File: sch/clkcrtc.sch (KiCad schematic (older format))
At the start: 26 parts, among them Q1 16 MHz, Q2 13.333 MHz

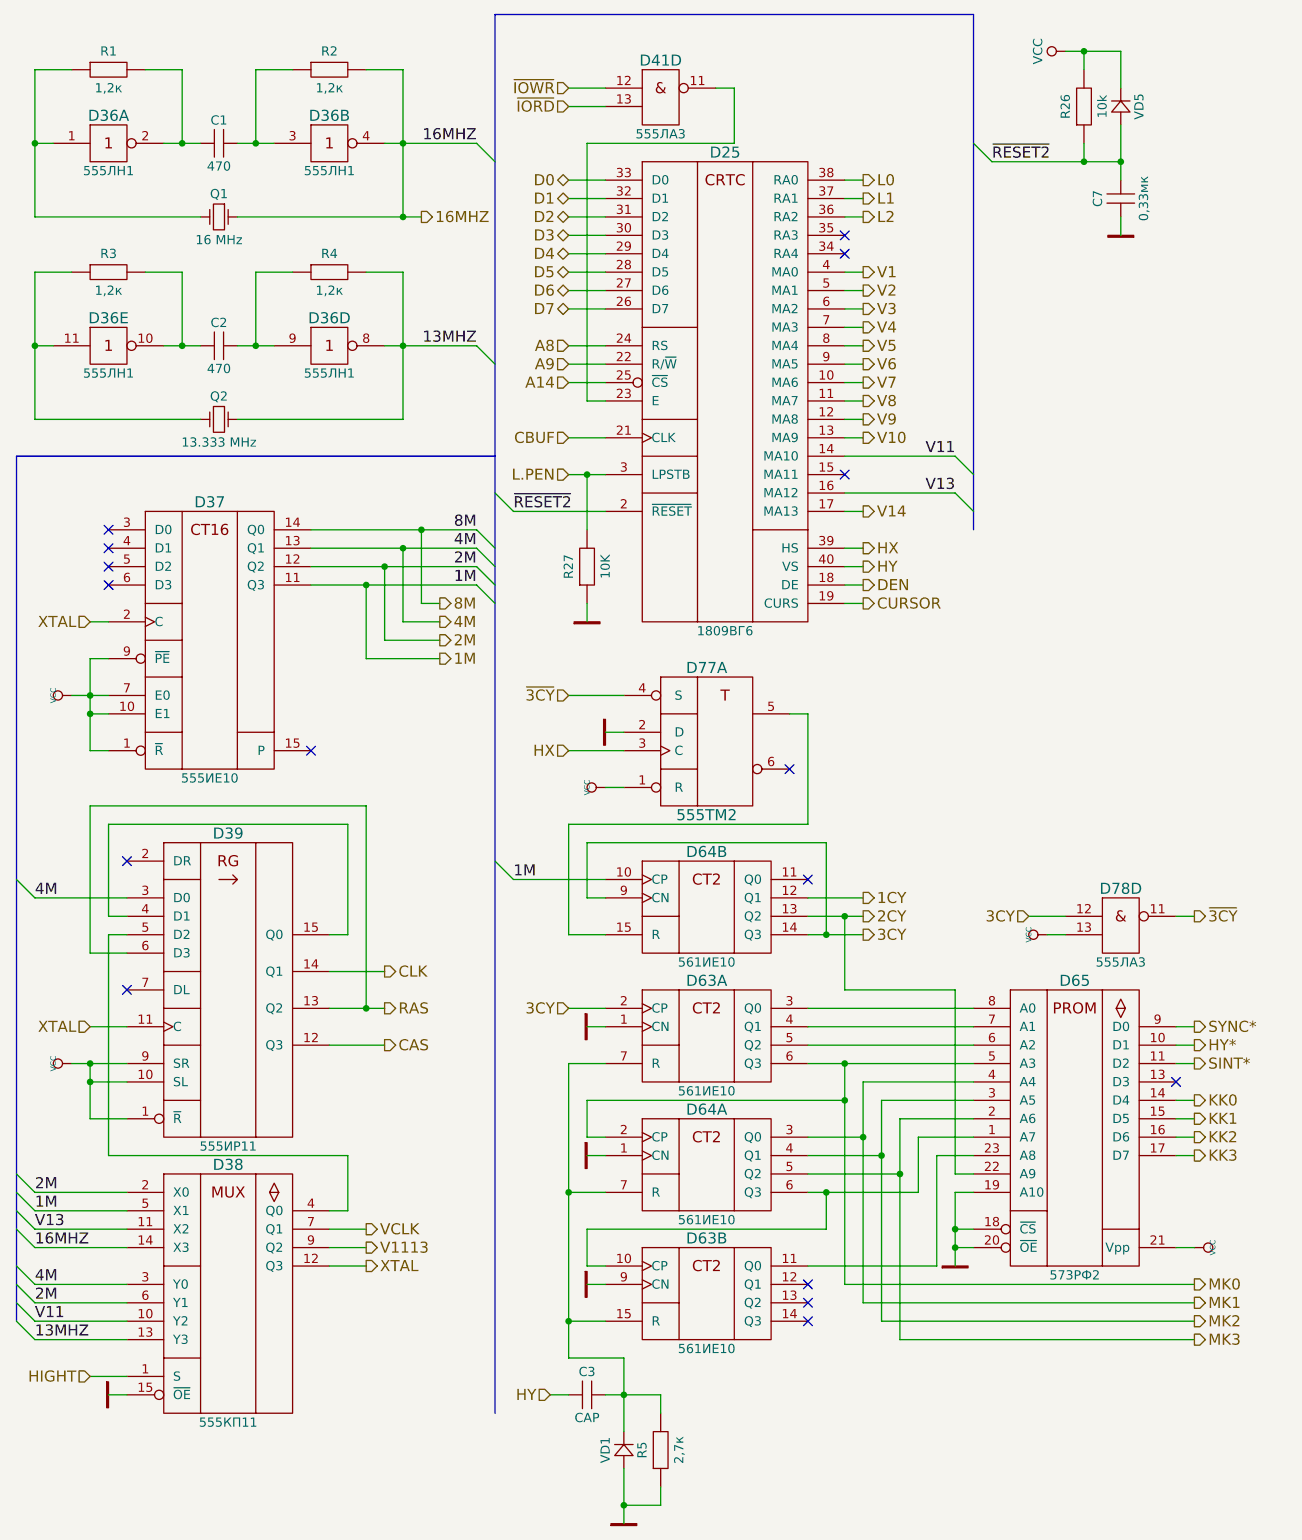
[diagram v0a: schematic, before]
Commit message: More precise version. PCB needs a lot of work.
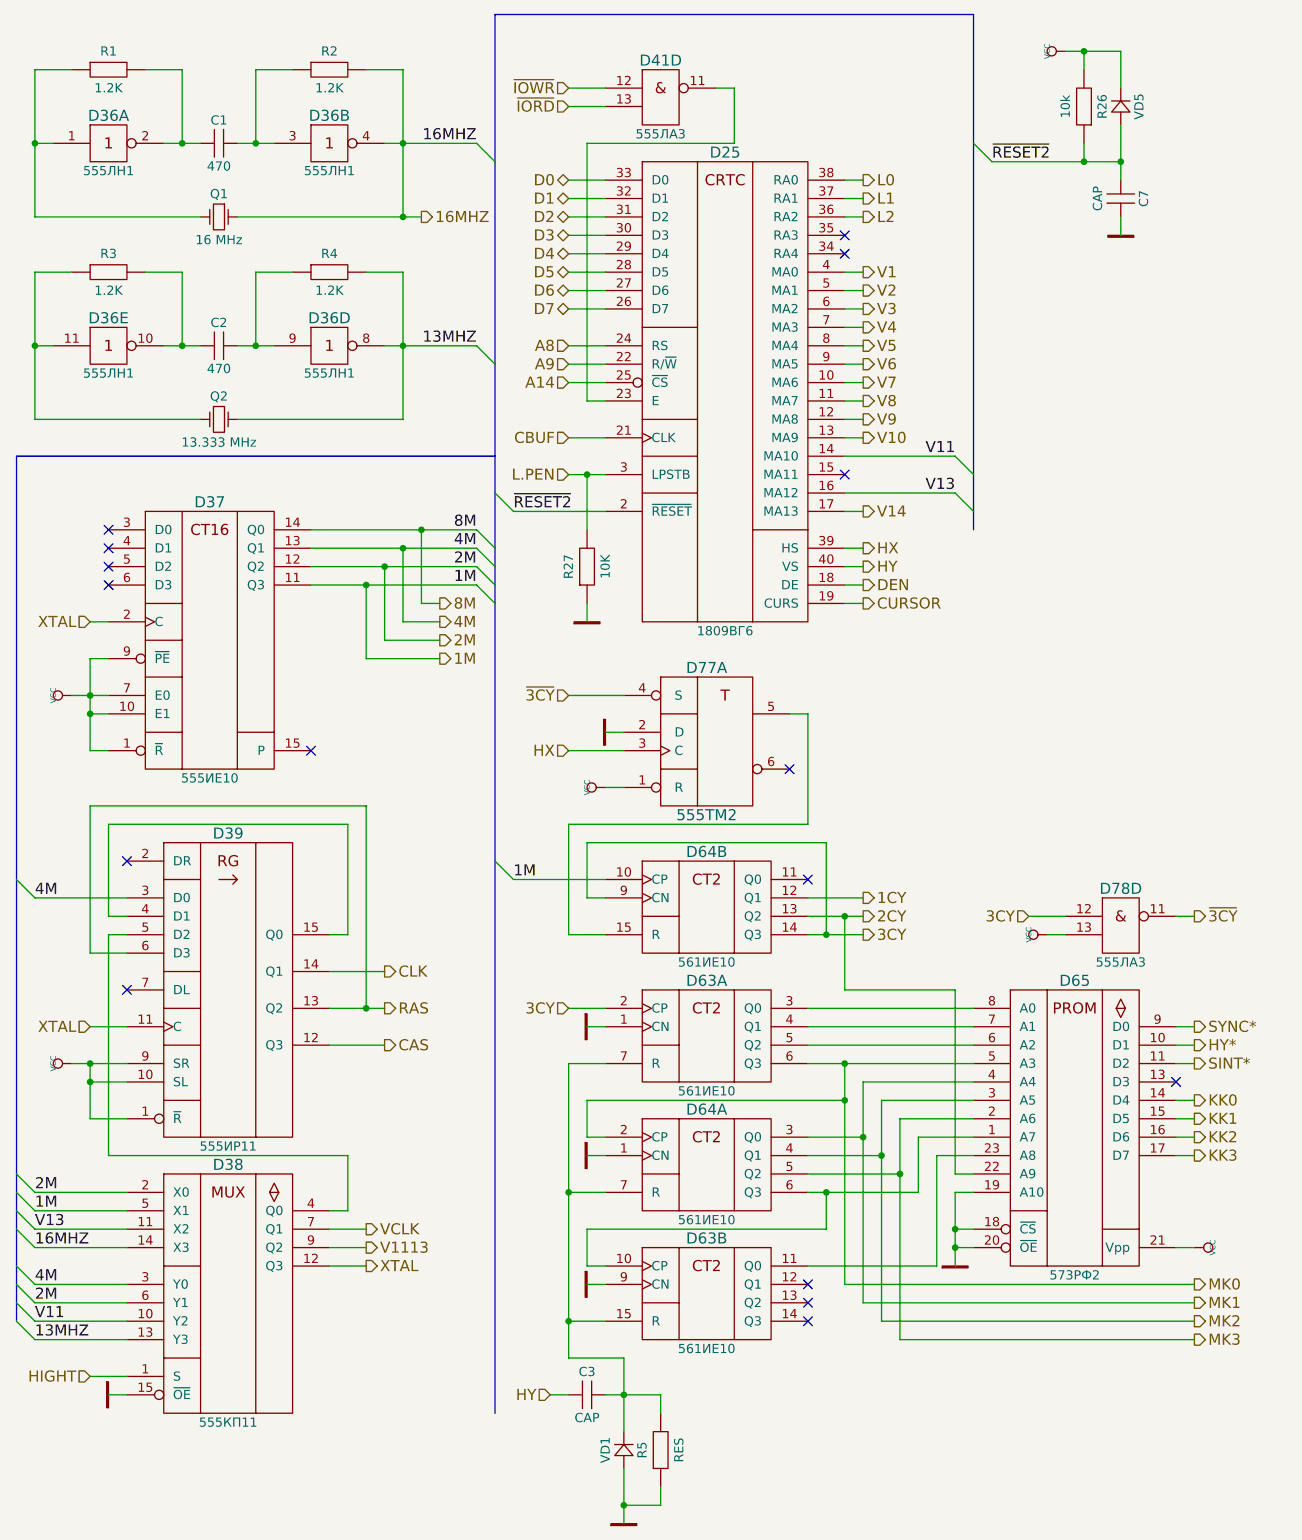
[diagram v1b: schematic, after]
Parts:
- C1, C2, C3: footprint MyLib:C_Disc_D7.5_P2.5 -> MyLib_metric:C_Disc_D7.5_P2.5
- C7: value 0,33мк -> CAP; footprint MyLib:C_Disc_D7.5_P2.5 -> MyLib_metric:C_Disc_D7.5_P2.5
- D25: footprint MyLib:DIP-40 -> MyLib_metric:DIP-40
- D36, D41, D77, D78: footprint MyLib:DIP-14 -> MyLib_metric:DIP-14
- D37, D38, D39, D63, D64: footprint MyLib:DIP-16 -> MyLib_metric:DIP-16
- D65: footprint MyLib:DIP-24 -> MyLib_metric:DIP-24
- R1, R2, R3, R4: value 1,2к -> 1.2K; footprint MyLib:Resistor_Horizontal_RM7.5mm -> MyLib_metric:Resistor_Horizontal_RM7.5mm
- R26, R27: footprint MyLib:Resistor_Horizontal_RM7.5mm -> MyLib_metric:Resistor_Horizontal_RM7.5mm
- R5: value 2,7к -> RES; footprint MyLib:Resistor_Horizontal_RM7.5mm -> MyLib_metric:Resistor_Horizontal_RM7.5mm
- VD1, VD5: footprint MyLib:Diode_DO-35_SOD27_Horizontal_RM7.5 -> MyLib_metric:Diode_DO-35_SOD27_Horizontal_RM7.5
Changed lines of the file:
@@
 F 0 "D36" H 1300 1650 60  0000 C CNN
 F 1 "555ЛН1" H 1300 1350 50  0000 C CNN
-F 2 "MyLib:DIP-14" H 1300 1450 60  0001 C CNN
+F 2 "MyLib_metric:DIP-14" H 1300 1450 60  0001 C CNN
 F 3 "" H 1300 1450 60  0000 C CNN
 	1    1300 1500
@@
 F 0 "D36" H 2500 1650 60  0000 C CNN
 F 1 "555ЛН1" H 2500 1350 50  0000 C CNN
-F 2 "MyLib:DIP-14" H 2500 1450 60  0001 C CNN
+F 2 "MyLib_metric:DIP-14" H 2500 1450 60  0001 C CNN
 F 3 "" H 2500 1450 60  0000 C CNN
 	2    2500 1500
@@
 F 0 "D36" H 1300 2750 60  0000 C CNN
 F 1 "555ЛН1" H 1300 2450 50  0000 C CNN
-F 2 "MyLib:DIP-14" H 1300 2550 60  0001 C CNN
+F 2 "MyLib_metric:DIP-14" H 1300 2550 60  0001 C CNN
 F 3 "" H 1300 2550 60  0000 C CNN
 	5    1300 2600
@@
 F 0 "D36" H 2500 2750 60  0000 C CNN
 F 1 "555ЛН1" H 2500 2450 50  0000 C CNN
-F 2 "MyLib:DIP-14" H 2500 2550 60  0001 C CNN
+F 2 "MyLib_metric:DIP-14" H 2500 2550 60  0001 C CNN
 F 3 "" H 2500 2550 60  0000 C CNN
 	4    2500 2600
@@
 P 1300 1100
 F 0 "R1" H 1300 1200 50  0000 C CNN
-F 1 "1,2к" H 1300 1000 50  0000 C CNN
-F 2 "MyLib:Resistor_Horizontal_RM7.5mm" H 1300 1050 60  0001 C CNN
+F 1 "1.2K" H 1300 1000 50  0000 C CNN
+F 2 "MyLib_metric:Resistor_Horizontal_RM7.5mm" H 1300 1050 60  0001 C CNN
 F 3 "" H 1300 1050 60  0000 C CNN
 	1    1300 1100
@@
 P 2500 1100
 F 0 "R2" H 2500 1200 50  0000 C CNN
-F 1 "1,2к" H 2500 1000 50  0000 C CNN
-F 2 "MyLib:Resistor_Horizontal_RM7.5mm" H 2500 1050 60  0001 C CNN
+F 1 "1.2K" H 2500 1000 50  0000 C CNN
+F 2 "MyLib_metric:Resistor_Horizontal_RM7.5mm" H 2500 1050 60  0001 C CNN
 F 3 "" H 2500 1050 60  0000 C CNN
 	1    2500 1100
@@
 F 0 "C1" H 1900 1625 50  0000 C CNN
 F 1 "470" H 1900 1375 50  0000 C CNN
-F 2 "MyLib:C_Disc_D7.5_P2.5" H 1900 1450 60  0001 C CNN
+F 2 "MyLib_metric:C_Disc_D7.5_P2.5" H 1900 1450 60  0001 C CNN
 F 3 "" H 1900 1450 60  0000 C CNN
 	1    1900 1500
@@
 P 1300 2200
 F 0 "R3" H 1300 2300 50  0000 C CNN
-F 1 "1,2к" H 1300 2100 50  0000 C CNN
-F 2 "MyLib:Resistor_Horizontal_RM7.5mm" H 1300 2150 60  0001 C CNN
+F 1 "1.2K" H 1300 2100 50  0000 C CNN
+F 2 "MyLib_metric:Resistor_Horizontal_RM7.5mm" H 1300 2150 60  0001 C CNN
 F 3 "" H 1300 2150 60  0000 C CNN
 	1    1300 2200
@@
 P 2500 2200
 F 0 "R4" H 2500 2300 50  0000 C CNN
-F 1 "1,2к" H 2500 2100 50  0000 C CNN
-F 2 "MyLib:Resistor_Horizontal_RM7.5mm" H 2500 2150 60  0001 C CNN
+F 1 "1.2K" H 2500 2100 50  0000 C CNN
+F 2 "MyLib_metric:Resistor_Horizontal_RM7.5mm" H 2500 2150 60  0001 C CNN
 F 3 "" H 2500 2150 60  0000 C CNN
 	1    2500 2200
@@
 F 0 "C2" H 1900 2725 50  0000 C CNN
 F 1 "470" H 1900 2475 50  0000 C CNN
-F 2 "MyLib:C_Disc_D7.5_P2.5" H 1900 2550 60  0001 C CNN
+F 2 "MyLib_metric:C_Disc_D7.5_P2.5" H 1900 2550 60  0001 C CNN
 F 3 "" H 1900 2550 60  0000 C CNN
 	1    1900 2600
@@
 F 0 "D37" H 1850 3750 60  0000 C CNN
 F 1 "555ИЕ10" H 1850 2250 50  0000 C CNN
-F 2 "MyLib:DIP-16" H 1600 3350 60  0001 C CNN
+F 2 "MyLib_metric:DIP-16" H 1600 3350 60  0001 C CNN
 F 3 "" H 1600 3350 60  0000 C CNN
 	1    1300 3600
@@
 F 0 "D38" H 1950 7350 60  0000 C CNN
 F 1 "555КП11" H 1950 5950 50  0000 C CNN
-F 2 "MyLib:DIP-16" H 1700 6950 60  0001 C CNN
+F 2 "MyLib_metric:DIP-16" H 1700 6950 60  0001 C CNN
 F 3 "" H 1700 6950 60  0000 C CNN
 	1    1400 7200
@@
 F 0 "D77" H 4550 4650 60  0000 C CNN
 F 1 "555ТМ2" H 4550 3850 60  0000 C CNN
-F 2 "MyLib:DIP-14" H 4400 4250 60  0001 C CNN
+F 2 "MyLib_metric:DIP-14" H 4400 4250 60  0001 C CNN
 F 3 "" H 4400 4250 60  0000 C CNN
 	1    4100 4500
@@
 F 0 "D64" H 4550 7050 60  0000 C CNN
 F 1 "561ИЕ10" H 4550 6450 50  0000 C CNN
-F 2 "MyLib:DIP-16" H 4300 6650 60  0001 C CNN
+F 2 "MyLib_metric:DIP-16" H 4300 6650 60  0001 C CNN
 F 3 "" H 4300 6650 60  0000 C CNN
 	1    4000 6900
@@
 F 0 "D63" H 4550 7750 60  0000 C CNN
 F 1 "561ИЕ10" H 4550 7150 50  0000 C CNN
-F 2 "MyLib:DIP-16" H 4300 7350 60  0001 C CNN
+F 2 "MyLib_metric:DIP-16" H 4300 7350 60  0001 C CNN
 F 3 "" H 4300 7350 60  0000 C CNN
 	2    4000 7600
@@
 F 0 "D63" H 4550 6350 60  0000 C CNN
 F 1 "561ИЕ10" H 4550 5750 50  0000 C CNN
-F 2 "MyLib:DIP-16" H 4300 5950 60  0001 C CNN
+F 2 "MyLib_metric:DIP-16" H 4300 5950 60  0001 C CNN
 F 3 "" H 4300 5950 60  0000 C CNN
 	1    4000 6200
@@
 F 0 "D64" H 4550 5650 60  0000 C CNN
 F 1 "561ИЕ10" H 4550 5050 50  0000 C CNN
-F 2 "MyLib:DIP-16" H 4300 5250 60  0001 C CNN
+F 2 "MyLib_metric:DIP-16" H 4300 5250 60  0001 C CNN
 F 3 "" H 4300 5250 60  0000 C CNN
 	2    4000 5500
@@
 F 0 "D65" H 6550 6350 60  0000 C CNN
 F 1 "573РФ2" H 6550 4750 50  0000 C CNN
-F 2 "MyLib:DIP-24" H 6300 5950 60  0001 C CNN
+F 2 "MyLib_metric:DIP-24" H 6300 5950 60  0001 C CNN
 F 3 "" H 6300 5950 60  0000 C CNN
 	1    6000 6200
@@
 F 0 "C3" H 3900 8425 50  0000 C CNN
 F 1 "CAP" H 3900 8175 50  0000 C CNN
-F 2 "MyLib:C_Disc_D7.5_P2.5" H 3900 8250 60  0001 C CNN
+F 2 "MyLib_metric:C_Disc_D7.5_P2.5" H 3900 8250 60  0001 C CNN
 F 3 "" H 3900 8250 60  0000 C CNN
 	1    3900 8300
@@
 F 0 "VD1" H 4100 8700 50  0000 C CNN
 F 1 "DIODE_MY" H 4100 8500 50  0001 C CNN
-F 2 "MyLib:Diode_DO-35_SOD27_Horizontal_RM7.5" H 4100 8550 60  0001 C CNN
+F 2 "MyLib_metric:Diode_DO-35_SOD27_Horizontal_RM7.5" H 4100 8550 60  0001 C CNN
 F 3 "" H 4100 8550 60  0000 C CNN
 	1    4100 8600
@@
 P 4300 8600
 F 0 "R5" H 4300 8700 50  0000 C CNN
-F 1 "2,7к" H 4300 8500 50  0000 C CNN
-F 2 "MyLib:Resistor_Horizontal_RM7.5mm" H 4300 8550 60  0001 C CNN
+F 1 "RES" H 4300 8500 50  0000 C CNN
+F 2 "MyLib_metric:Resistor_Horizontal_RM7.5mm" H 4300 8550 60  0001 C CNN
 F 3 "" H 4300 8550 60  0000 C CNN
 	1    4300 8600
@@
 F 0 "D39" H 1950 5550 60  0000 C CNN
 F 1 "555ИР11" H 1950 3850 50  0000 C CNN
-F 2 "MyLib:DIP-16" H 1700 5350 60  0001 C CNN
+F 2 "MyLib_metric:DIP-16" H 1700 5350 60  0001 C CNN
 F 3 "" H 1700 5350 60  0000 C CNN
 	1    1400 5400
@@
 F 0 "D78" H 6800 5850 60  0000 C CNN
 F 1 "555ЛА3" H 6800 5450 50  0000 C CNN
-F 2 "MyLib:DIP-14" H 6800 5650 60  0001 C CNN
+F 2 "MyLib_metric:DIP-14" H 6800 5650 60  0001 C CNN
 F 3 "" H 6800 5650 60  0000 C CNN
 	4    6800 5700
@@
 F 0 "D25" H 4650 1850 60  0000 C CNN
 F 1 "1809ВГ6" H 4650 -750 50  0000 C CNN
-F 2 "MyLib:DIP-40" H 4300 1450 60  0001 C CNN
+F 2 "MyLib_metric:DIP-40" H 4300 1450 60  0001 C CNN
 F 3 "" H 4300 1450 60  0000 C CNN
 	1    4000 1700
@@
 F 0 "D41" H 4300 1350 60  0000 C CNN
 F 1 "555ЛА3" H 4300 950 50  0000 C CNN
-F 2 "MyLib:DIP-14" H 4300 1150 60  0001 C CNN
+F 2 "MyLib_metric:DIP-14" H 4300 1150 60  0001 C CNN
 F 3 "" H 4300 1150 60  0000 C CNN
 	4    4300 1200
@@
 F 0 "VD5" H 6800 1400 50  0000 C CNN
 F 1 "DIODE_MY" H 6800 1200 50  0001 C CNN
-F 2 "MyLib:Diode_DO-35_SOD27_Horizontal_RM7.5" H 6800 1250 60  0001 C CNN
+F 2 "MyLib_metric:Diode_DO-35_SOD27_Horizontal_RM7.5" H 6800 1250 60  0001 C CNN
 F 3 "" H 6800 1250 60  0000 C CNN
 	1    6800 1300
@@
 F 0 "R26" H 6600 1400 50  0000 C CNN
 F 1 "10k" H 6600 1200 50  0000 C CNN
-F 2 "MyLib:Resistor_Horizontal_RM7.5mm" H 6600 1250 60  0001 C CNN
+F 2 "MyLib_metric:Resistor_Horizontal_RM7.5mm" H 6600 1250 60  0001 C CNN
 F 3 "" H 6600 1250 60  0000 C CNN
 	1    6600 1300
-	0    -1   -1   0
+	0    1    -1   0
 $EndComp
 $Comp
@@
 P 6800 1800
 F 0 "C7" H 6800 1925 50  0000 C CNN
-F 1 "0,33мк" H 6800 1675 50  0000 C CNN
-F 2 "MyLib:C_Disc_D7.5_P2.5" H 6800 1750 60  0001 C CNN
+F 1 "CAP" H 6800 1675 50  0000 C CNN
+F 2 "MyLib_metric:C_Disc_D7.5_P2.5" H 6800 1750 60  0001 C CNN
 F 3 "" H 6800 1750 60  0000 C CNN
 	1    6800 1800
-	0    -1   -1   0
-$EndComp
-$Comp
-L GND #PWR0132
+	0    1    -1   0
+$EndComp
+$Comp
+L VCC #PWR0132
+U 1 1 566D560C
+P 6500 1000
+F 0 "#PWR0132" H 6500 1100 30  0001 C CNN
+F 1 "VCC" H 6500 1100 30  0000 C CNN
+F 2 "" H 6500 1000 60  0000 C CNN
+F 3 "" H 6500 1000 60  0000 C CNN
+	1    6500 1000
+	0    -1   1    0
+$EndComp
+$Comp
+L GND #PWR0133
 U 1 1 566D5786
 P 6800 2000
-F 0 "#PWR0132" H 6800 2000 30  0001 C CNN
+F 0 "#PWR0133" H 6800 2000 30  0001 C CNN
 F 1 "GND" H 6800 1930 30  0001 C CNN
 F 2 "" H 6800 2000 60  0000 C CNN
@@
 F 0 "R27" H 3900 3900 50  0000 C CNN
 F 1 "10K" H 3900 3700 50  0000 C CNN
-F 2 "MyLib:Resistor_Horizontal_RM7.5mm" H 3900 3750 60  0001 C CNN
+F 2 "MyLib_metric:Resistor_Horizontal_RM7.5mm" H 3900 3750 60  0001 C CNN
 F 3 "" H 3900 3750 60  0000 C CNN
 	1    3900 3800
@@
 $EndComp
 $Comp
-L GND #PWR0133
+L GND #PWR0134
 U 1 1 566D6741
 P 3900 4100
-F 0 "#PWR0133" H 3900 4100 30  0001 C CNN
+F 0 "#PWR0134" H 3900 4100 30  0001 C CNN
 F 1 "GND" H 3900 4030 30  0001 C CNN
 F 2 "" H 3900 4100 60  0000 C CNN
@@
 Connection ~ 2800 3800
 $Comp
-L GND #PWR0134
+L GND #PWR0135
 U 1 1 5673CA75
 P 3900 7700
-F 0 "#PWR0134" H 3900 7700 30  0001 C CNN
+F 0 "#PWR0135" H 3900 7700 30  0001 C CNN
 F 1 "GND" H 3900 7630 30  0001 C CNN
 F 2 "" H 3900 7700 60  0000 C CNN
@@
 	2700 4300 2700 3900
 Connection ~ 2700 3900
-$Comp
-L VCC #PWR0135
-U 1 1 56E2031B
-P 6500 1000
-F 0 "#PWR0135" H 6500 850 50  0001 C CNN
-F 1 "VCC" H 6500 1150 50  0000 C CNN
-F 2 "" H 6500 1000 50  0000 C CNN
-F 3 "" H 6500 1000 50  0000 C CNN
-	1    6500 1000
-	0    -1   -1   0
-$EndComp
 $EndSCHEMATC
